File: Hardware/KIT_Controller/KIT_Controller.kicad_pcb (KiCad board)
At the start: 2 copper layers, 115.8 x 99.2 mm, 45 parts, among them J201 USB_B, J202 USB_BOOT, SW101 TM1000, U101 Nokia_5110_LCD, U202 W25Q128JVS, U203 NCP1117-3.3_SOT223, U205 RP2040, U301 CC1101, Y201 Crystal

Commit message: bump libs and squeeze into shape
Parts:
- removed H102, H103, H104, H105: MountingHole_Pad, MountingHole:MountingHole_2.5mm_Pad_TopBottom
- added C102: EBM15DSEH, KenwoodFox:Lewis_Card_Connector, F.Cu at (150.0, 150.0)
- moved C202 28.9 mm to (139.1, 64.0)
- moved C207 28.9 mm to (154.1, 51.2)
- moved C210 28.9 mm to (139.1, 58.0)
- moved C215 28.9 mm to (154.1, 54.2)
- moved R203 28.9 mm to (162.9, 51.1)
- moved U203 28.9 mm to (137.5, 71.4)
- moved C214 28.9 mm to (139.1, 61.0)
- moved C203 28.9 mm to (152.4, 61.4)
- moved C204 28.9 mm to (143.5, 58.0)
- moved C213 28.9 mm to (143.5, 64.0)
- moved J201 28.9 mm to (120.8, 57.2)
- moved J202 28.9 mm to (149.5, 52.0)
- moved R103 28.9 mm to (120.1, 84.0)
- moved R104 28.9 mm to (124.5, 84.0)
- moved R201 28.9 mm to (124.5, 75.0)
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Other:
- board size 115.8 x 99.2 mm -> 75 x 116.7 mm

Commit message: Bump
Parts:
- removed H101: MountingHole_Pad, MountingHole:MountingHole_2.5mm_Pad_TopBottom
- moved D103 33.7 mm to (158.3, 107.8), turned to 180 degrees
- moved D102 29.3 mm to (145.3, 107.8), turned to 180 degrees
- moved D101 29.0 mm to (158.3, 145.2), turned to 180 degrees
- moved C101 25.8 mm to (127.0, 128.9)
- moved D104 23.7 mm to (145.3, 145.2), turned to 180 degrees
- moved U101 20.4 mm to (132.2, 126.5), turned to 90 degrees
- moved JP101 13.6 mm to (138.5, 123.2), turned to 90 degrees

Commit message: Add gnd and cleanup
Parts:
- removed J201: USB_B, Connector_USB:USB_B_OST_USB-B1HSxx_Horizontal
- added H101: MountingHole_Pad, MountingHole:MountingHole_2.5mm_Pad_TopBottom, F.Cu at (178.0, 138.5)
- added H102: MountingHole_Pad, MountingHole:MountingHole_2.5mm_Pad_TopBottom, F.Cu at (120.0, 138.0)
- added J203: USBC, Connector_USB:USB_C_Receptacle_XKB_U262-16XN-4BVC11, F.Cu at (131.0, 44.5)
- added R206: 5K1, Resistor_SMD:R_0805_2012Metric, F.Cu at (127.4, 50.7)
- added R207: 5K1, Resistor_SMD:R_0805_2012Metric, F.Cu at (127.4, 53.6)
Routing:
- added copper zone on B.Cu, net GND
- added copper zone on F.Cu, net GND

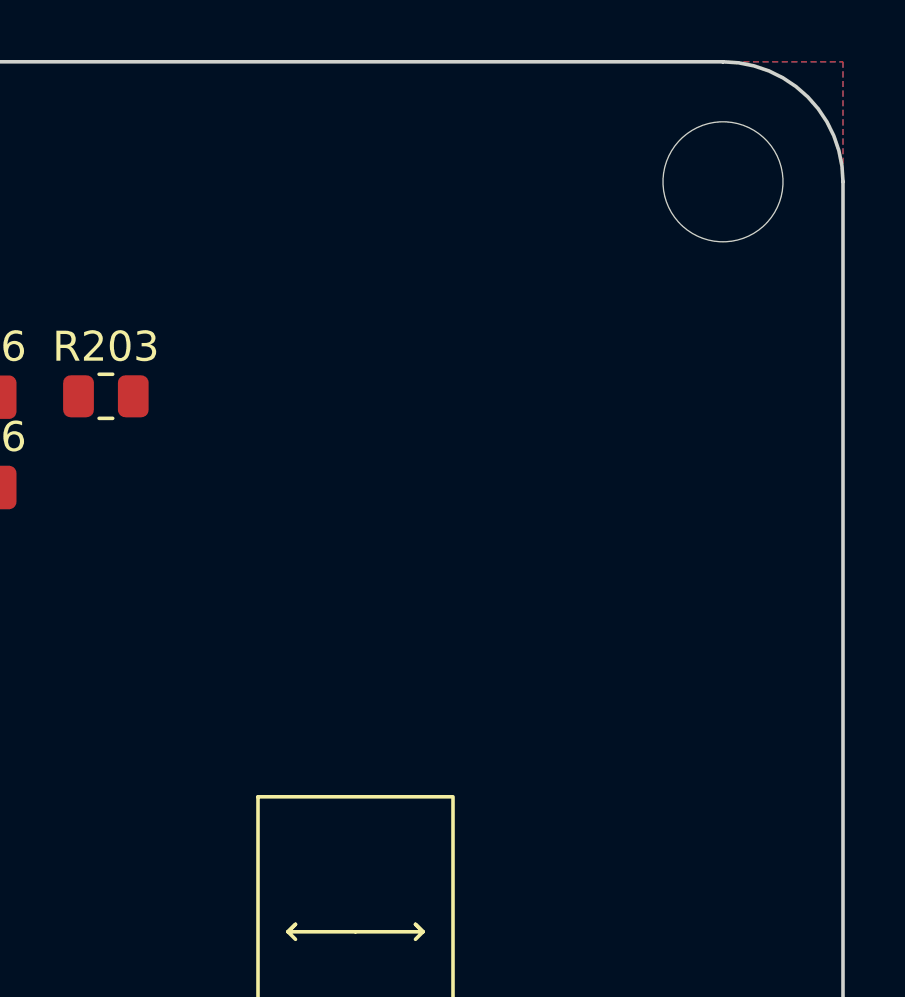
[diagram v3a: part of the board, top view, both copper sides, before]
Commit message: Add SD cardg
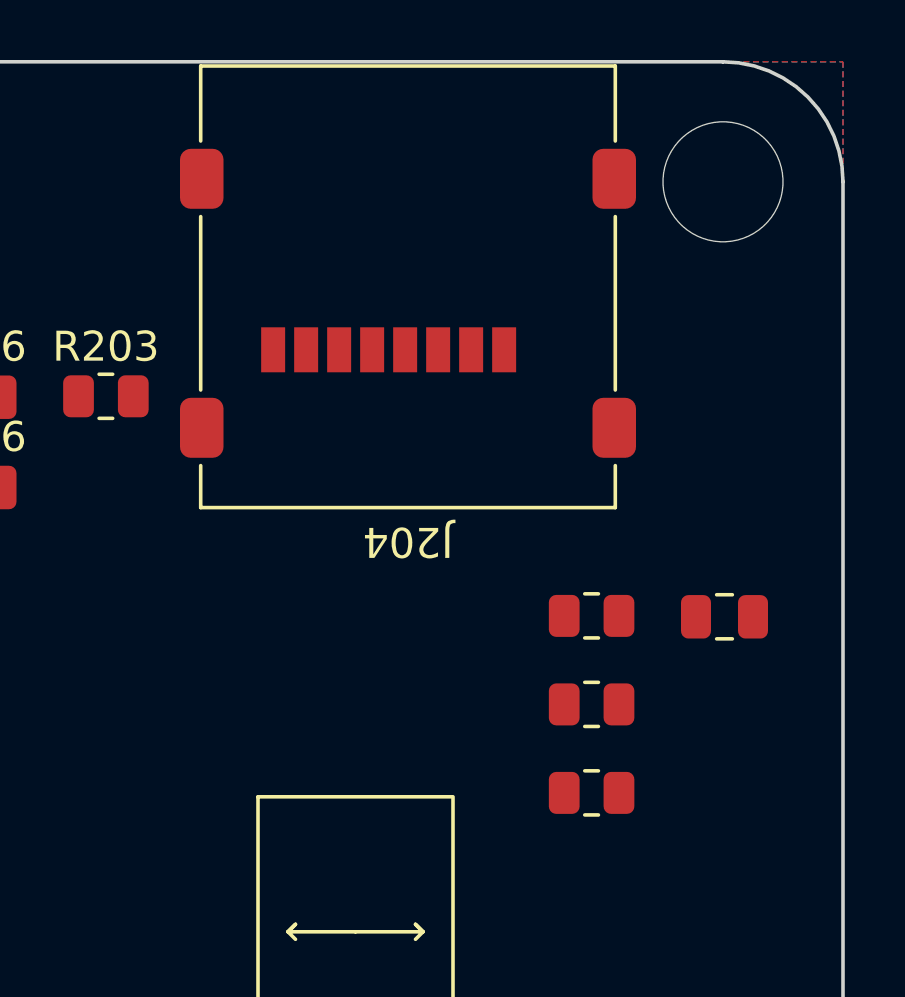
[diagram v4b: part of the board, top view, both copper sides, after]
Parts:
- added C217: 10u, Capacitor_SMD:C_0805_2012Metric, F.Cu at (183.6, 58.5)
- added J204: Micro_SD_Card, Connector_Card:microSD_HC_Molex_47219-2001, F.Cu at (173.0, 47.5)
- added R208: 10K, Resistor_SMD:R_0805_2012Metric, F.Cu at (179.1, 58.5)
- added R209: 10K, Resistor_SMD:R_0805_2012Metric, F.Cu at (179.1, 61.4)
- added R210: DNF, Resistor_SMD:R_0805_2012Metric, F.Cu at (179.1, 64.4)
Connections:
- U205 pad 31: unconnected-(U205-GPIO20-Pad31) -> /MCU/SD_CMD
- U205 pad 32: unconnected-(U205-GPIO21-Pad32) -> /MCU/SD_DAT0
- U205 pad 34: unconnected-(U205-GPIO22-Pad34) -> /MCU/SD_DAT1
- U205 pad 35: unconnected-(U205-GPIO23-Pad35) -> /MCU/SD_DAT2
- U205 pad 36: unconnected-(U205-GPIO24-Pad36) -> /MCU/SD_DAT3
- U205 pad 8: unconnected-(U205-GPIO6-Pad8) -> /MCU/SD_CLK

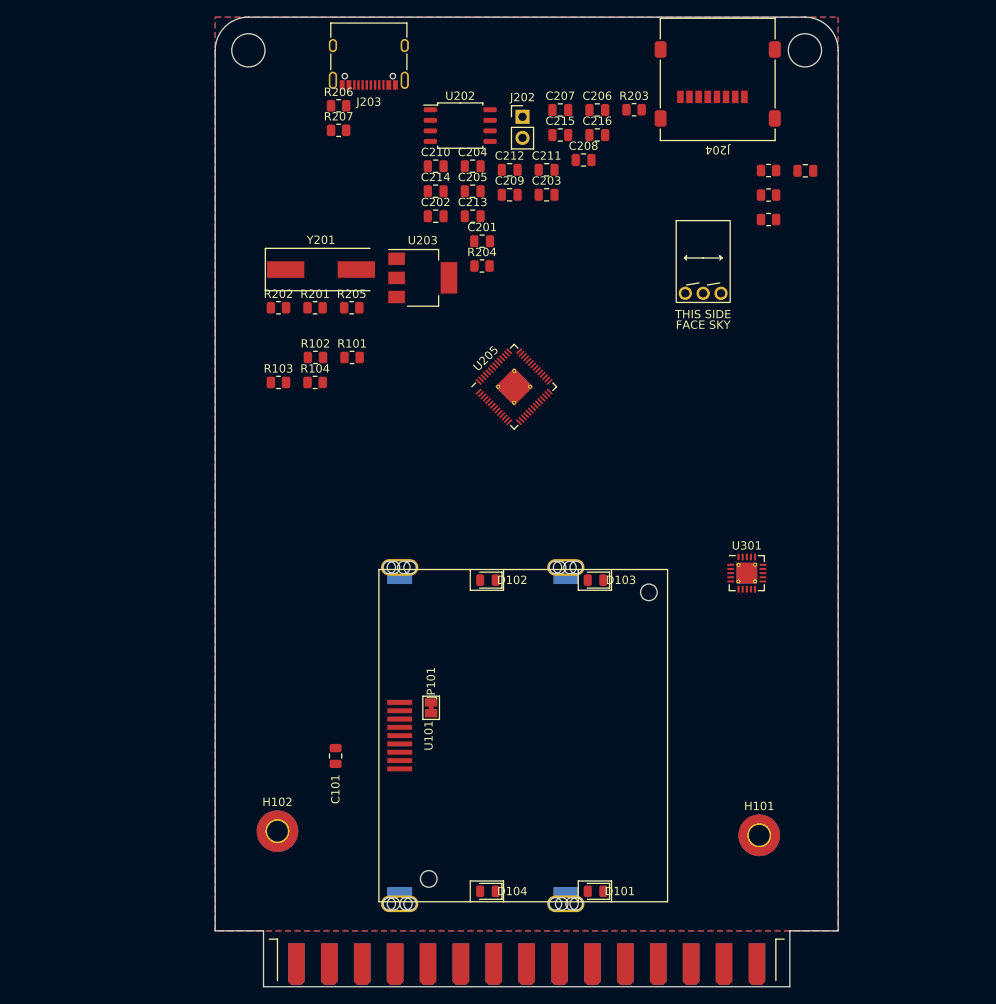
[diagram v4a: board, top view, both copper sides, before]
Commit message: include upstream fixes in kit controller
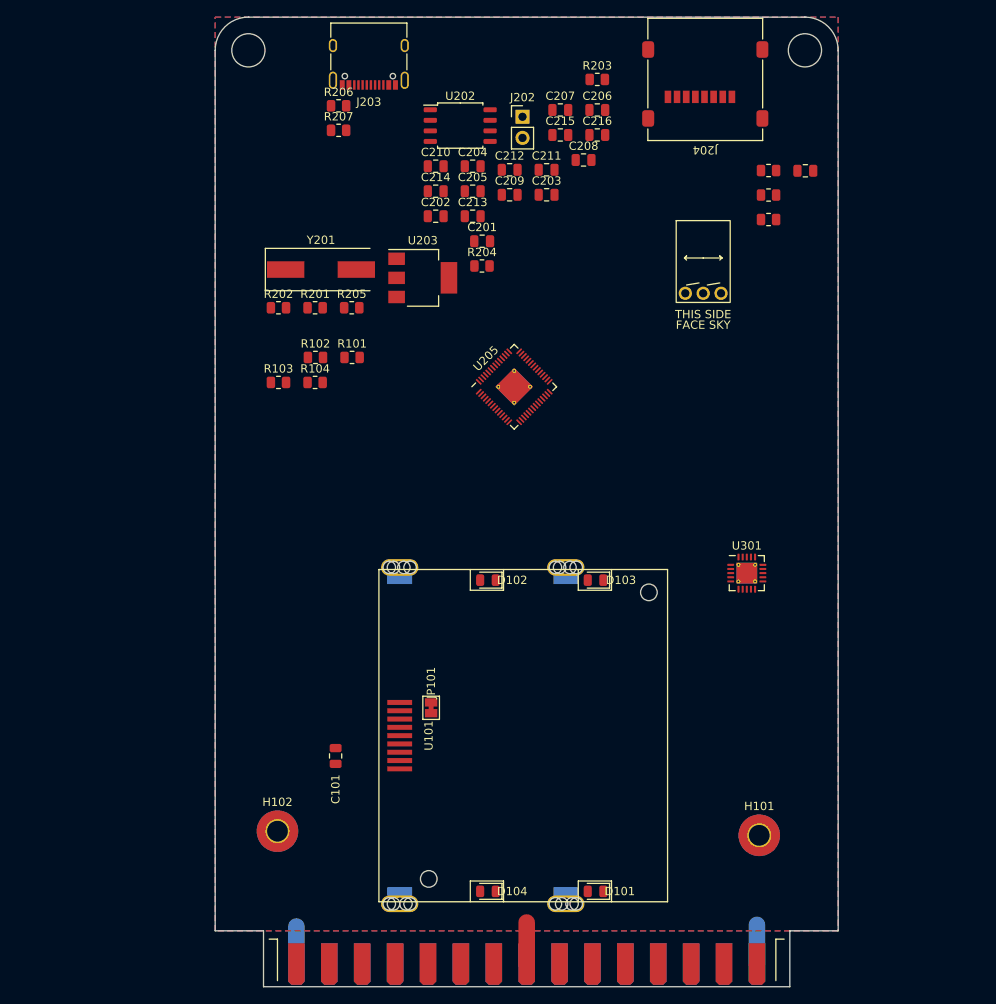
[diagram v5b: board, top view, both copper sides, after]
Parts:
- removed C102: EBM15DSEH, KenwoodFox:Lewis_Card_Connector
- added U102: CARD ?, KenwoodFox:Lewis_Card_Connector, F.Cu at (150.0, 150.0)
- moved R203 5.74 mm to (158.5, 47.5)
- moved J204 1.50 mm to (171.5, 47.5)
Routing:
- net GND: track 0.00 -> 14.2 mm

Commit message: Add stuff
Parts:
- removed J204: Micro_SD_Card, Connector_Card:microSD_HC_Molex_47219-2001
- added J201: Micro_SD_Card_Det1, Connector_Card:microSD_HC_Molex_104031-0811, F.Cu at (171.5, 46.6)
- added R215: DNP, Resistor_SMD:R_0805_2012Metric, F.Cu at (181.0, 54.4)
- added R216: DNP, Resistor_SMD:R_0805_2012Metric, F.Cu at (181.0, 51.5)
- added R217: DNP, Resistor_SMD:R_0805_2012Metric, F.Cu at (181.0, 48.5)

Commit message: Bump to new ver
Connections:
- U102 pad 11: unconnected-(U102-I2C_SCL-Pad11) -> /SCL
- U102 pad 13: unconnected-(U102-I2C_SDA-Pad13) -> /SDA
- U205 pad 6: /MCU/SDA -> /SDA
- U205 pad 7: /MCU/SCL -> /SCL
